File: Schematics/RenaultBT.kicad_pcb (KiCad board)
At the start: 2 copper layers, 160 x 100.3 mm, 63 parts, among them J1 PowerSupply, J2 SPDIF_Output, J3 HU_CDC_Interface, J4 Screw_Terminal_01x02, J5 Screw_Terminal_01x03, J6 Screw_Terminal_01x03, Q1 2N7000, Q2 2N7000, Q3 2N7000, Q4 2N7000, U1 LM2575-5.0BT, U2 LM3940, U3 WM8804, U4 CSRA64215, U5 74HC04, U6 STM32F103, Y1 12Mhz

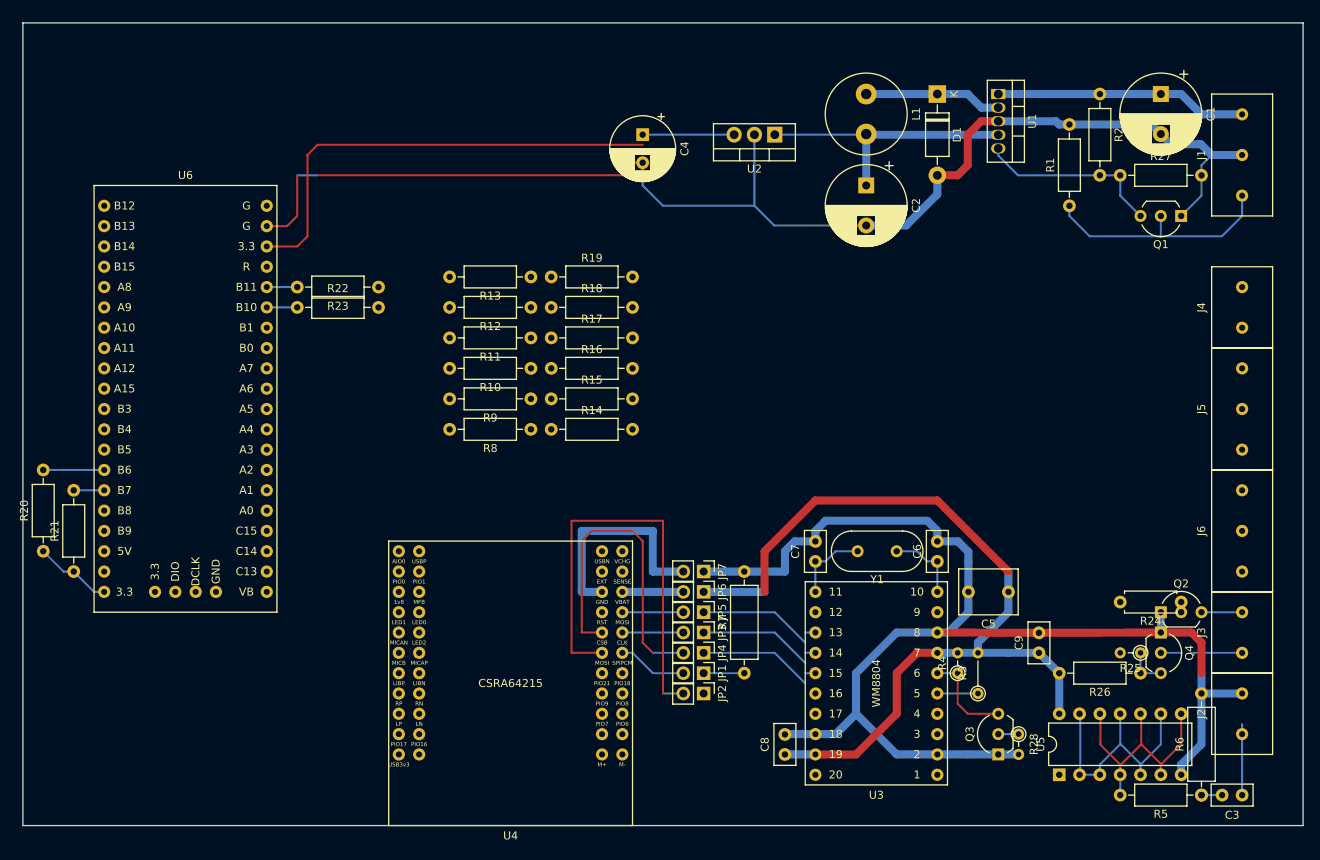
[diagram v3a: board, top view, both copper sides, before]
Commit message: Fixed voltage level issues between BT module and WM8804; fixed CDC Emulator hw interface; modified PCB design
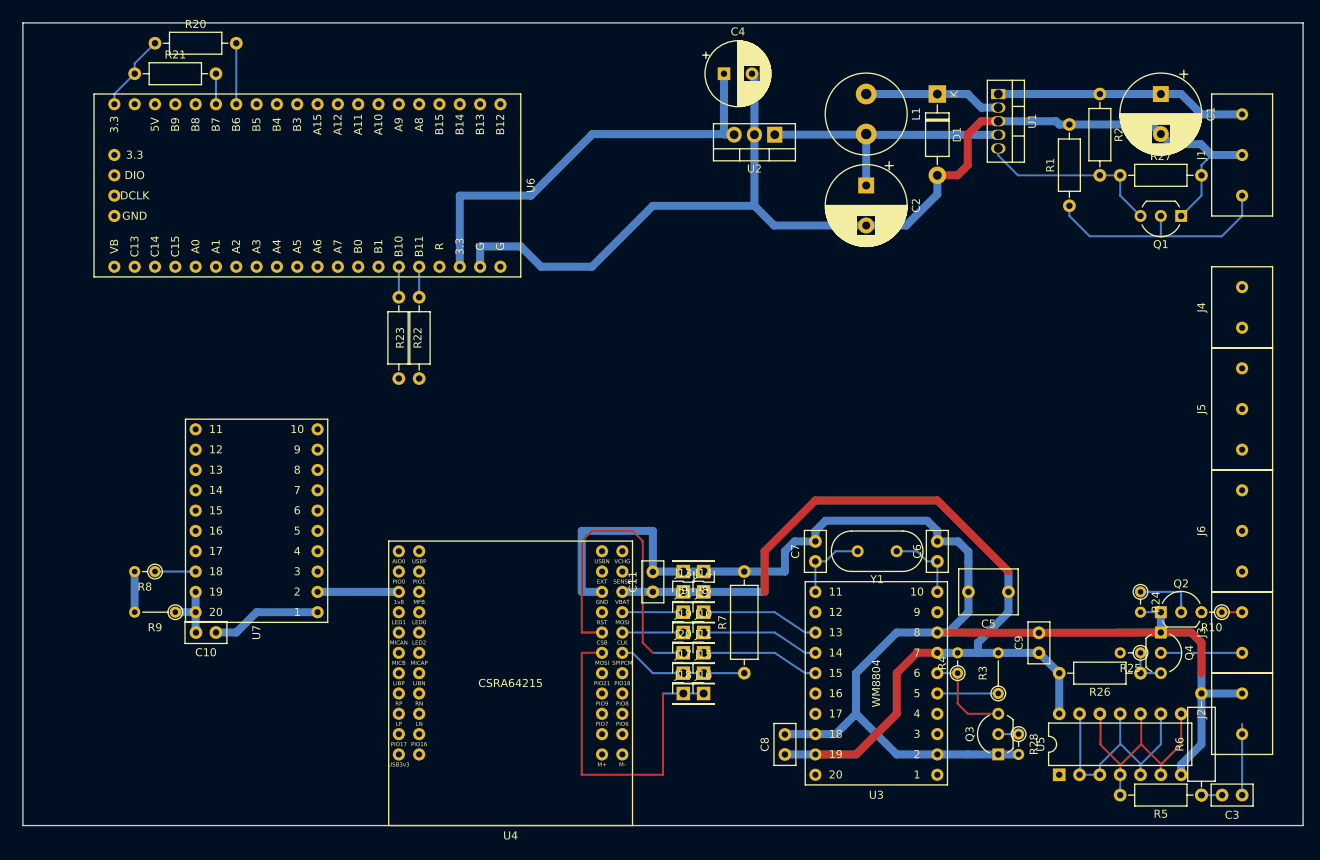
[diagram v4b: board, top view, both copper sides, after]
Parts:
- removed JP1, JP2, JP3, JP4, JP5, JP6, JP7: Jumper, Connector_PinHeader_2.54mm:PinHeader_1x02_P2.54mm_Vertical
- removed R11, R12, R13: 10k, Resistor_THT:R_Axial_DIN0207_L6.3mm_D2.5mm_P10.16mm_Horizontal
- removed R14, R15, R16, R17, R18, R19: 12k, Resistor_THT:R_Axial_DIN0207_L6.3mm_D2.5mm_P10.16mm_Horizontal
- added C10: 0.1uF, Capacitor_THT:C_Disc_D5.0mm_W2.5mm_P2.50mm, F.Cu at (74.9, 114.3)
- added C11: 0.1uF, Capacitor_THT:C_Disc_D5.0mm_W2.5mm_P2.50mm, F.Cu at (129.5, 109.2)
- added J10: Conn_01x01_Male, Connector_PinHeader_2.54mm:PinHeader_1x01_P2.54mm_Vertical, F.Cu at (135.9, 114.3)
- added J11: Conn_01x01_Male, Connector_PinHeader_2.54mm:PinHeader_1x01_P2.54mm_Vertical, F.Cu at (135.9, 116.8)
- added J12: Conn_01x01_Male, Connector_PinHeader_2.54mm:PinHeader_1x01_P2.54mm_Vertical, F.Cu at (135.9, 111.8)
- added J13: Conn_01x01_Male, Connector_PinHeader_2.54mm:PinHeader_1x01_P2.54mm_Vertical, F.Cu at (133.3, 109.2)
- added J14: Conn_01x01_Male, Connector_PinHeader_2.54mm:PinHeader_1x01_P2.54mm_Vertical, F.Cu at (135.9, 109.2)
- added J15: Conn_01x01_Male, Connector_PinHeader_2.54mm:PinHeader_1x01_P2.54mm_Vertical, F.Cu at (135.9, 119.4)
- added J16: Conn_01x01_Male, Connector_PinHeader_2.54mm:PinHeader_1x01_P2.54mm_Vertical, F.Cu at (135.9, 121.9)
- added J17: Conn_01x01_Male, Connector_PinHeader_2.54mm:PinHeader_1x01_P2.54mm_Vertical, F.Cu at (133.3, 119.4)
- added J18: Conn_01x01_Male, Connector_PinHeader_2.54mm:PinHeader_1x01_P2.54mm_Vertical, F.Cu at (133.3, 121.9)
- added J19: Conn_01x01_Male, Connector_PinHeader_2.54mm:PinHeader_1x01_P2.54mm_Vertical, F.Cu at (133.3, 114.3)
- added J20: Conn_01x01_Male, Connector_PinHeader_2.54mm:PinHeader_1x01_P2.54mm_Vertical, F.Cu at (133.3, 116.8)
- added J21: Conn_01x01_Male, Connector_PinHeader_2.54mm:PinHeader_1x01_P2.54mm_Vertical, F.Cu at (133.3, 111.8)
- added J8: Conn_01x01_Male, Connector_PinHeader_2.54mm:PinHeader_1x01_P2.54mm_Vertical, F.Cu at (135.9, 106.7)
- added J9: Conn_01x01_Male, Connector_PinHeader_2.54mm:PinHeader_1x01_P2.54mm_Vertical, F.Cu at (133.3, 106.7)
- added U7: GTL2003, GTL2003:GTL2003, F.Cu at (80.0, 100.3)
- R10: value 10k -> 470; footprint Resistor_THT:R_Axial_DIN0207_L6.3mm_D2.5mm_P10.16mm_Horizontal -> Resistor_THT:R_Axial_DIN0204_L3.6mm_D1.6mm_P2.54mm_Vertical
- R24: value 100 -> 10K; footprint Resistor_THT:R_Axial_DIN0207_L6.3mm_D2.5mm_P7.62mm_Horizontal -> Resistor_THT:R_Axial_DIN0204_L3.6mm_D1.6mm_P2.54mm_Vertical
- R8: value 10k -> 330; footprint Resistor_THT:R_Axial_DIN0207_L6.3mm_D2.5mm_P10.16mm_Horizontal -> Resistor_THT:R_Axial_DIN0204_L3.6mm_D1.6mm_P2.54mm_Vertical
- R9: value 10k -> 200K; footprint Resistor_THT:R_Axial_DIN0207_L6.3mm_D2.5mm_P10.16mm_Horizontal -> Resistor_THT:R_Axial_DIN0204_L3.6mm_D1.6mm_P5.08mm_Vertical
- moved R10 91.6 mm to (200.7, 111.8)
- moved R20 65.0 mm to (67.3, 40.6), turned to 0 degrees
- moved R21 62.7 mm to (64.8, 44.5), turned to 0 degrees
- moved R9 51.8 mm to (69.8, 111.8)
- moved R8 50.2 mm to (67.3, 106.7)
- moved U6 30.7 mm to (86.4, 58.4), turned to 270 degrees
- moved R22 12.8 mm to (97.8, 72.4), turned to 270 degrees
- moved C4 12.7 mm to (138.4, 44.5), turned to 0 degrees
- moved R23 12.5 mm to (100.3, 82.5), turned to 90 degrees
- moved R24 5.24 mm to (190.5, 109.2), turned to 270 degrees
- moved R3 2.54 mm to (172.7, 121.9)
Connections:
- Q2 pad 2: Net-(Q2-Pad2) -> /HU_CDC_InterfaceAdapter/CDC_TX
- Q2 pad 3: /HU_CDC_InterfaceAdapter/HU_RX -> Net-(Q2-Pad3)
- R10 pad 1: /BTModule/BTModule_ButtonIF_3v3Divider/OUT_PIO8 -> /HU_CDC_InterfaceAdapter/HU_RX
- R10 pad 2: (no net) -> Net-(Q2-Pad3)
- R24 pad 1: Net-(Q2-Pad2) -> /HU_CDC_InterfaceAdapter/CDC_TX
- R24 pad 2: /HU_CDC_InterfaceAdapter/CDC_TX -> /I2SToSPDIF/DGND
- R7 pad 1: Net-(JP1-Pad1) -> Net-(J15-Pad1)
- R8 pad 1: /BTModule/BTModule_ButtonIF_3v3Divider/OUT_PIO6 -> /I2SToSPDIF/I2S_SD_IN
- R8 pad 2: (no net) -> /BTModule/3V3
- R9 pad 1: /BTModule/BTModule_ButtonIF_3v3Divider/OUT_PIO7 -> Net-(C10-Pad2)
- R9 pad 2: (no net) -> /BTModule/3V3
- U4 pad 10: /BTModule/BTModule_ButtonIF_3v3Divider/OUT_PIO21 -> (no net)
- U4 pad 11: Net-(JP1-Pad2) -> Net-(J15-Pad1)
- U4 pad 17: Net-(JP6-Pad2) -> /BTModule/3V3
- U4 pad 18: Net-(JP7-Pad2) -> /I2SToSPDIF/DGND
- U4 pad 28: (no net) -> Net-(U4-Pad28)
- U4 pad 5: /BTModule/BTModule_ButtonIF_3v3Divider/OUT_PIO6 -> (no net)
- U4 pad 6: /BTModule/BTModule_ButtonIF_3v3Divider/OUT_PIO7 -> (no net)
- U4 pad 7: /BTModule/BTModule_ButtonIF_3v3Divider/OUT_PIO8 -> (no net)
- U4 pad 8: /BTModule/BTModule_ButtonIF_3v3Divider/OUT_PIO9 -> (no net)
- U4 pad 9: /BTModule/BTModule_ButtonIF_3v3Divider/OUT_PIO18 -> (no net)
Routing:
- net Net-(JP7-Pad2): track 27.9 -> 0.00 mm
- net /I2SToSPDIF/DGND: track 319.1 -> 346.8 mm
- net /HU_CDC_InterfaceAdapter/3V3: track 179.5 -> 156.2 mm
- net /BTModule/3V3: track 0.00 -> 22.9 mm
- net Net-(J15-Pad1): track 0.00 -> 16.3 mm
- net Net-(J16-Pad1): track 55.9 -> 43.2 mm
- net Net-(U4-Pad28): track 0.00 -> 10.2 mm
- net /HU_CDC_InterfaceAdapter/CDC_TX: track 0.00 -> 8.89 mm
- net Net-(JP1-Pad2): track 8.67 -> 0.00 mm
- net Net-(C10-Pad2): track 0.00 -> 7.64 mm
- net Net-(JP6-Pad2): track 7.62 -> 0.00 mm
- net Net-(JP1-Pad1): track 5.08 -> 0.00 mm
- net /I2SToSPDIF/I2S_SD_IN: track 15.5 -> 19.8 mm
- net Net-(R3-Pad1): track 5.08 -> 7.62 mm
- net /HU_CDC_InterfaceAdapter/HU_RX: track 5.08 -> 2.54 mm
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
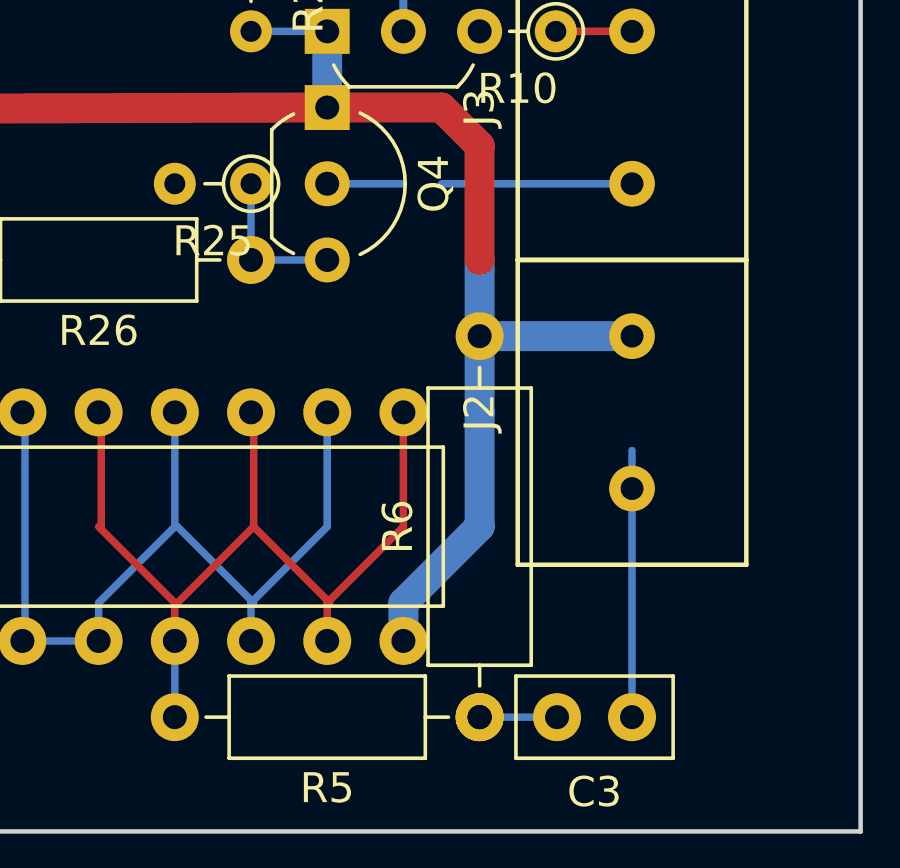
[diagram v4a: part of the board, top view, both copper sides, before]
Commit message: Updated schematic and PCB design (minor modifications on layout)
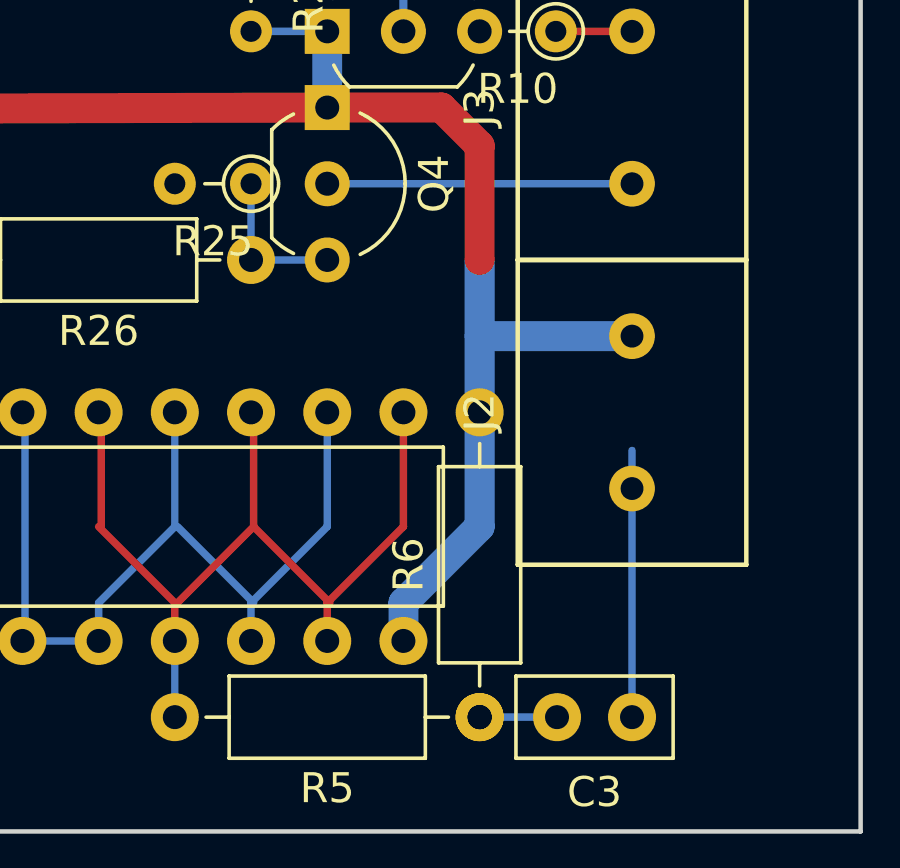
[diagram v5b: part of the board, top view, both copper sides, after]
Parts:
- R6: footprint Resistor_THT:R_Axial_DIN0309_L9.0mm_D3.2mm_P12.70mm_Horizontal -> Resistor_THT:R_Axial_DIN0207_L6.3mm_D2.5mm_P10.16mm_Horizontal
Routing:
- net /HU_CDC_InterfaceAdapter/HU_TX: track 8.89 -> 10.2 mm
